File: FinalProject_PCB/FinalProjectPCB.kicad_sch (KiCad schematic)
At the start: 18 parts, among them J1 SerialJack, J2 Conn_01x09, SW1 SW_Push_Dual, SW2 SW_Push_Dual, SW3 SW_Push_Dual, SW4 SW_Push_Dual, SW5 SW_Push_Dual, SW6 SW_Push_Dual, SW7 SW_SPST, SW8 SW_Push_Dual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

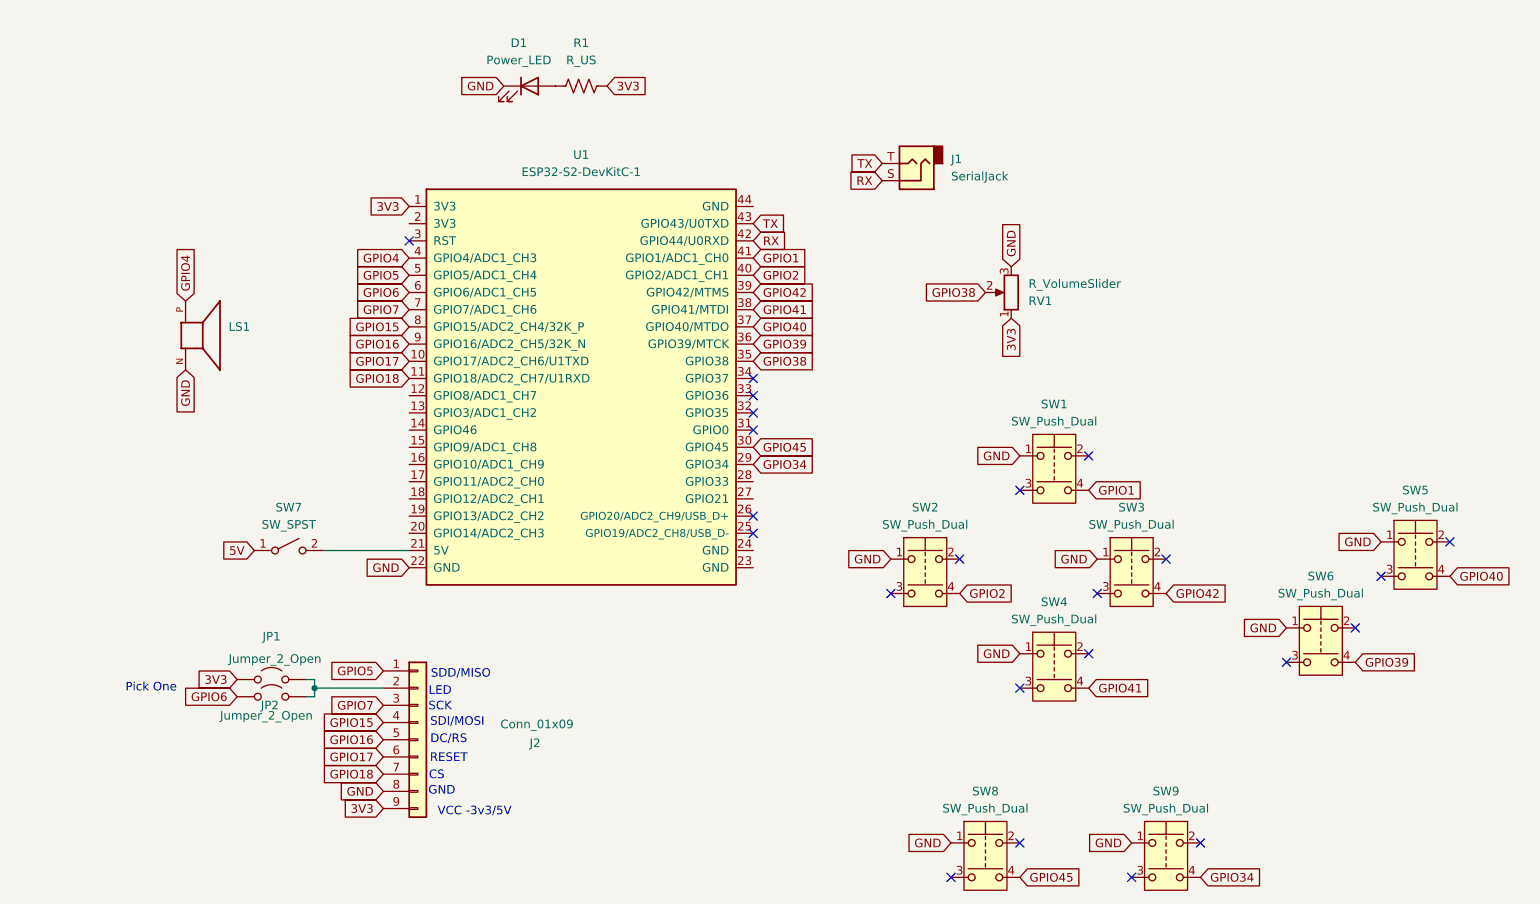
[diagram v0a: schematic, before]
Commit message: added GND pin to serial
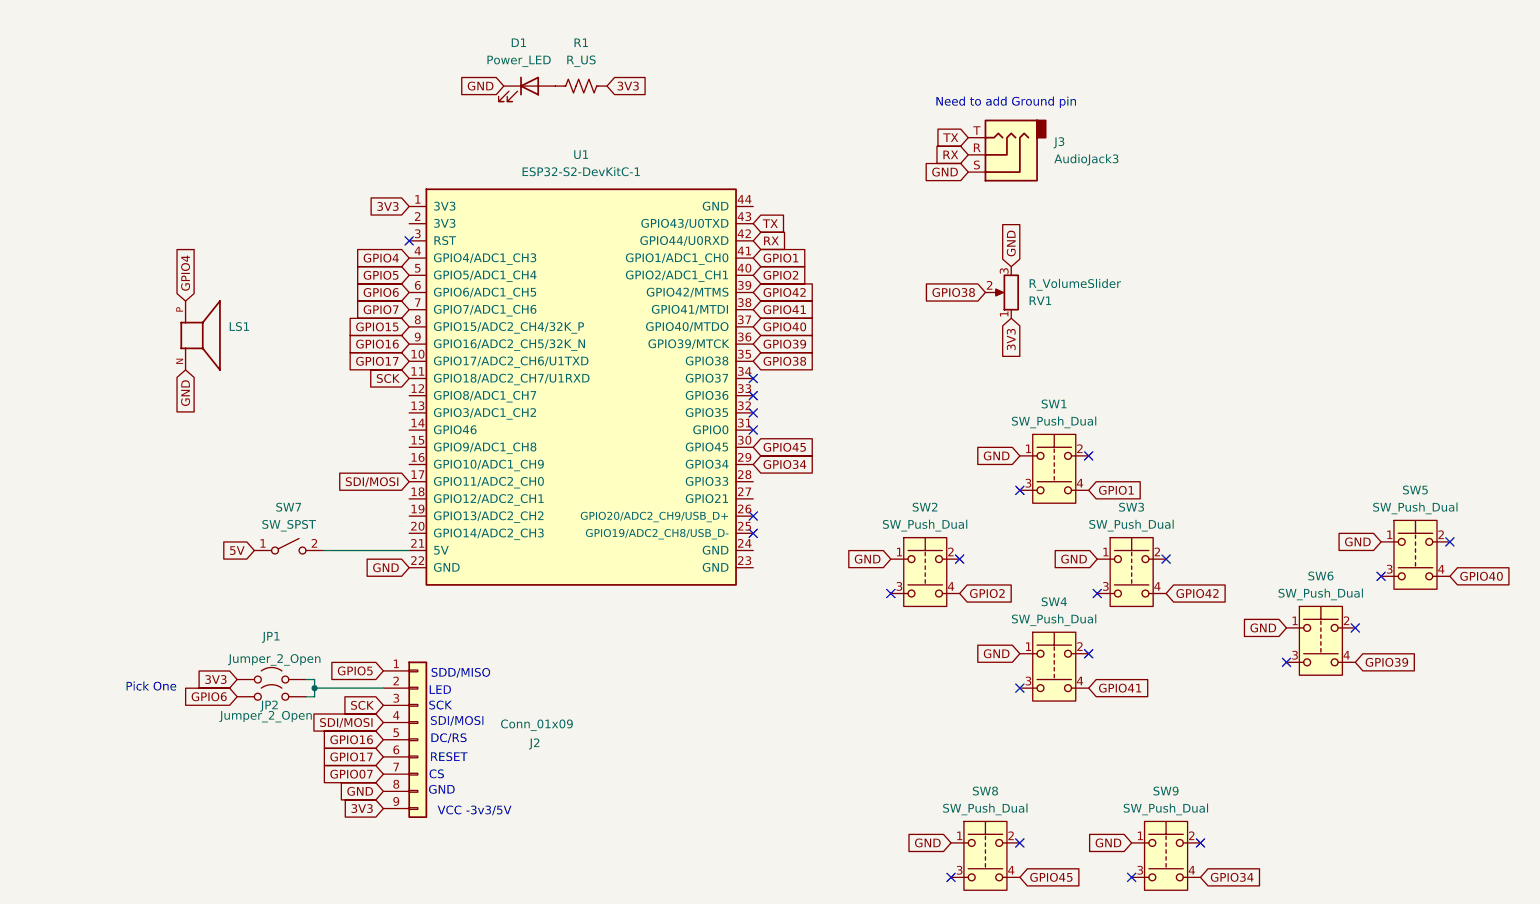
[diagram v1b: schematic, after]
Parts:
- removed J1: SerialJack, symbol Connector_Audio:AudioJack2
- added J3: AudioJack3, symbol Connector_Audio:AudioJack3
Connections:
- net GND: now also J3.S
- net GPIO15: no longer J2.4 (Pin_4)
- net GPIO7: no longer J2.3 (Pin_3)
- net RX: now also J3.R
- net TX: now also J3.T
- net SDI/MOSI: now reaches U1.17 (GPIO11/ADC2_CH0)
- net SDI/MOSI: now also J2.4 (Pin_4)
- net GPIO18 renamed GPIO07
- net GPIO07: no longer U1.11 (GPIO18/ADC2_CH7/U1RXD)
- new net SCK: J2.3 (Pin_3), U1.11 (GPIO18/ADC2_CH7/U1RXD)
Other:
- note added: "Need to add Ground pin"
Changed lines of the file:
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@@
+		)
+	)
+	(text "Need to add Ground pin"
+		(exclude_from_sim no)
+		(at 169.418 40.64 0)
+		(effects
+			(font
+				(size 1.27 1.27)
+			)
 		)
 	)
@@
 	(global_label "RX"
 		(shape input)
-		(at 151.13 52.07 180)
-		(fields_autoplaced yes)
-		(effects
-			(font
-				(size 1.27 1.27)
-			)
-			(justify right)
-		)
-		(property "Intersheetrefs" "${INTERSHEET_REFS}"
-			(at 145.6653 52.07 0)
+		(at 163.83 48.26 180)
+		(fields_autoplaced yes)
+		(effects
+			(font
+				(size 1.27 1.27)
+			)
+			(justify right)
+		)
+		(property "Intersheetrefs" "${INTERSHEET_REFS}"
+			(at 158.3653 48.26 0)
 			(effects
 				(font
@@
 		)
 	)
+	(global_label "SCK"
+		(shape input)
+		(at 81.28 81.28 180)
+		(fields_autoplaced yes)
+		(effects
+			(font
+				(size 1.27 1.27)
+			)
+			(justify right)
+		)
+		(property "Intersheetrefs" "${INTERSHEET_REFS}"
+			(at 74.5453 81.28 0)
+			(effects
+				(font
+					(size 1.27 1.27)
+				)
+				(justify right)
+				(hide yes)
+			)
+		)
+	)
 	(global_label "3V3"
 		(shape input)
@@
 		)
 	)
-	(global_label "GPIO18"
+	(global_label "GPIO07"
 		(shape input)
 		(at 77.47 139.7 180)
@@
 		)
 	)
-	(global_label "GPIO18"
-		(shape input)
-		(at 81.28 81.28 180)
-		(fields_autoplaced yes)
-		(effects
-			(font
-				(size 1.27 1.27)
-			)
-			(justify right)
-		)
-		(property "Intersheetrefs" "${INTERSHEET_REFS}"
-			(at 71.4005 81.28 0)
-			(effects
-				(font
-					(size 1.27 1.27)
-				)
-				(justify right)
-				(hide yes)
-			)
-		)
-	)
 	(global_label "TX"
 		(shape input)
-		(at 151.13 49.53 180)
-		(fields_autoplaced yes)
-		(effects
-			(font
-				(size 1.27 1.27)
-			)
-			(justify right)
-		)
-		(property "Intersheetrefs" "${INTERSHEET_REFS}"
-			(at 145.9677 49.53 0)
+		(at 163.83 45.72 180)
+		(fields_autoplaced yes)
+		(effects
+			(font
+				(size 1.27 1.27)
+			)
+			(justify right)
+		)
+		(property "Intersheetrefs" "${INTERSHEET_REFS}"
+			(at 158.6677 45.72 0)
 			(effects
 				(font
@@
 		)
 	)
+	(global_label "SDI{slash}MOSI"
+		(shape input)
+		(at 81.28 96.52 180)
+		(fields_autoplaced yes)
+		(effects
+			(font
+				(size 1.27 1.27)
+			)
+			(justify right)
+		)
+		(property "Intersheetrefs" "${INTERSHEET_REFS}"
+			(at 69.2838 96.52 0)
+			(effects
+				(font
+					(size 1.27 1.27)
+				)
+				(justify right)
+				(hide yes)
+			)
+		)
+	)
 	(global_label "GPIO4"
 		(shape input)
@@
 		)
 	)
+	(global_label "GND"
+		(shape input)
+		(at 163.83 50.8 180)
+		(fields_autoplaced yes)
+		(effects
+			(font
+				(size 1.27 1.27)
+			)
+			(justify right)
+		)
+		(property "Intersheetrefs" "${INTERSHEET_REFS}"
+			(at 156.9743 50.8 0)
+			(effects
+				(font
+					(size 1.27 1.27)
+				)
+				(justify right)
+				(hide yes)
+			)
+		)
+	)
 	(global_label "GPIO1"
 		(shape input)
@@
 		)
 	)
-	(global_label "GPIO7"
+	(global_label "SCK"
 		(shape input)
 		(at 77.47 129.54 180)
@@
 		)
 		(property "Intersheetrefs" "${INTERSHEET_REFS}"
-			(at 68.8 129.54 0)
-			(effects
-				(font
-					(size 1.27 1.27)
-				)
-				(justify right)
-				(hide yes)
-			)
-		)
-	)
-	(global_label "GPIO15"
+			(at 70.7353 129.54 0)
+			(effects
+				(font
+					(size 1.27 1.27)
+				)
+				(justify right)
+				(hide yes)
+			)
+		)
+	)
+	(global_label "SDI{slash}MOSI"
 		(shape input)
 		(at 77.47 132.08 180)
@@
 		)
 		(property "Intersheetrefs" "${INTERSHEET_REFS}"
-			(at 67.5905 132.08 0)
+			(at 65.4738 132.08 0)
 			(effects
 				(font
@@
 	)
 	(symbol
+		(lib_id "Connector_Audio:AudioJack3")
+		(at 168.91 48.26 180)
+		(unit 1)
+		(exclude_from_sim no)
+		(in_bom yes)
+		(on_board yes)
+		(dnp no)
+		(fields_autoplaced yes)
+		(property "Reference" "J3"
+			(at 176.53 46.3549 0)
+			(effects
+				(font
+					(size 1.27 1.27)
+				)
+				(justify right)
+			)
+		)
+		(property "Value" "AudioJack3"
+			(at 176.53 48.8949 0)
+			(effects
+				(font
+					(size 1.27 1.27)
+				)
+				(justify right)
+			)
+		)
+		(property "Footprint" ""
+			(at 168.91 48.26 0)
+			(effects
+				(font
+					(size 1.27 1.27)
+				)
+				(hide yes)
+			)
+		)
+		(property "Datasheet" "~"
+			(at 168.91 48.26 0)
+			(effects
+				(font
+					(size 1.27 1.27)
+				)
+				(hide yes)
+			)
+		)
+		(property "Description" "Audio Jack, 3 Poles (Stereo / TRS)"
+			(at 168.91 48.26 0)
+			(effects
+				(font
+					(size 1.27 1.27)
+				)
+				(hide yes)
+			)
+		)
+		(pin "R"
+		)
+		(pin "S"
+		)
+		(pin "T"
+		)
+		(instances
+			(project ""
+				(path "/779a3c99-a5a8-445d-8f38-e1d85c7e87cc"
+					(reference "J3")
+					(unit 1)
+				)
+			)
+		)
+	)
+	(symbol
 		(lib_id "Switch:SW_Push_Dual")
 		(at 229.87 107.95 0)
@@
 					(unit 1)
 				)
-			)
-		)
-	)
-	(symbol
-		(lib_id "Connector_Audio:AudioJack2")
-		(at 156.21 49.53 180)
-		(unit 1)
-		(exclude_from_sim no)
-		(in_bom yes)
-		(on_board yes)
-		(dnp no)
-		(fields_autoplaced yes)
-		(property "Reference" "J1"
-			(at 161.29 48.8949 0)
-			(effects
-				(font
-					(size 1.27 1.27)
-				)
-				(justify right)
-			)
-		)
-		(property "Value" "SerialJack"
-			(at 161.29 51.4349 0)
-			(effects
-				(font
-					(size 1.27 1.27)
-				)
-				(justify right)
-			)
-		)
-		(property "Footprint" ""
-			(at 156.21 49.53 0)
-			(effects
-				(font
-					(size 1.27 1.27)
-				)
-				(hide yes)
-			)
-		)
-		(property "Datasheet" "~"
-			(at 156.21 49.53 0)
-			(effects
-				(font
-					(size 1.27 1.27)
-				)
-				(hide yes)
-			)
-		)
-		(property "Description" "Audio Jack, 2 Poles (Mono / TS)"
-			(at 156.21 49.53 0)
-			(effects
-				(font
-					(size 1.27 1.27)
-				)
-				(hide yes)
-			)
-		)
-		(pin "T"
-		)
-		(pin "S"
-		)
-		(instances
-			(project ""
-				(path "/779a3c99-a5a8-445d-8f38-e1d85c7e87cc"
-					(reference "J1")
-					(unit 1)
-				)

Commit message: Updated Schematic to match working board
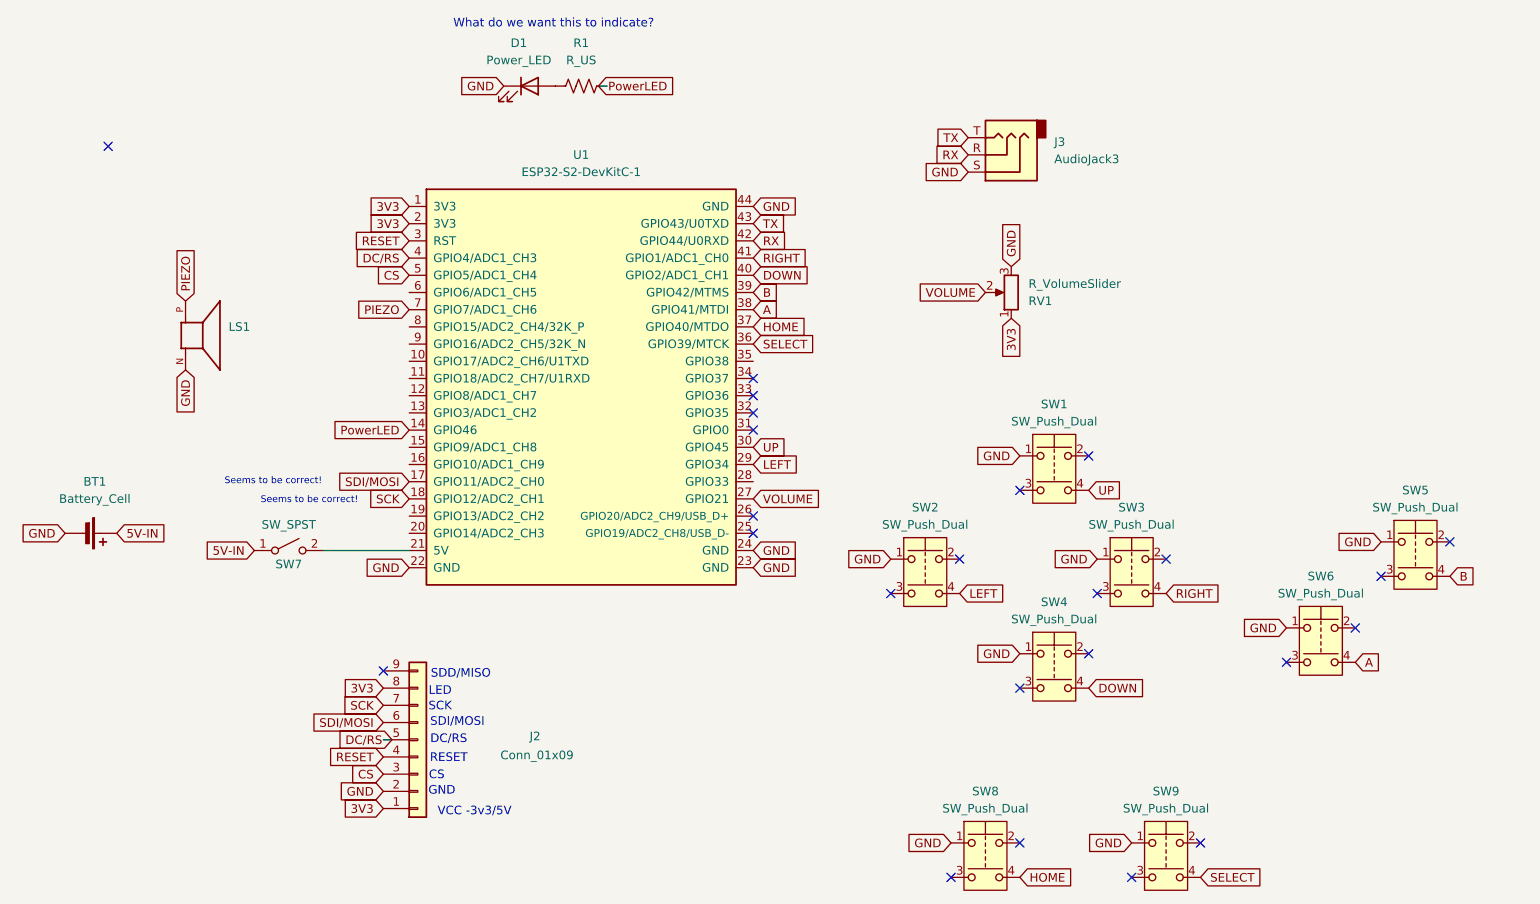
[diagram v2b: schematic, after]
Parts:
- removed JP1, JP2: Jumper_2_Open, symbol Jumper:Jumper_2_Open
- added BT1: Battery_Cell, symbol Device:Battery_Cell
- J2: footprint (none) -> TerminalBlock:TerminalBlock_Xinya_XY308-2.54-9P_1x09_P2.54mm_Horizontal
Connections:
- net GPIO07 is gone; now on net SCK: J2.7 (Pin_7)
- net 3V3: now also J2.1 (Pin_1), J2.8 (Pin_8), U1.2 (3V3); no longer J2.9 (Pin_9), R1.2
- net GND: now also J2.2 (Pin_2), U1.23 (GND), U1.24 (GND), U1.44 (GND), BT1.2 (-); no longer J2.8 (Pin_8)
- net SCK: now also U1.18 (GPIO12/ADC2_CH1); no longer J2.3 (Pin_3), U1.11 (GPIO18/ADC2_CH7/U1RXD)
- net SDI/MOSI: now also J2.6 (Pin_6); no longer J2.4 (Pin_4)
- net PowerLED: now reaches U1.14 (GPIO46)
- net PowerLED: now also R1.2
- net VOLUME: now reaches U1.27 (GPIO21)
- net VOLUME: now also RV1.2
- net RESET: now reaches U1.3 (RST)
- net RESET: now also J2.4 (Pin_4)
- net 5V renamed 5V-IN
- net 5V-IN: now also BT1.1 (+)
- net GPIO1 renamed RIGHT
- net RIGHT: now also SW3.4; no longer SW1.4
- net GPIO15: no longer names the net of U1.8 (GPIO15/ADC2_CH4/32K_P)
- net GPIO16: no longer names the net of U1.9 (GPIO16/ADC2_CH5/32K_N)
- net GPIO16: no longer J2.5 (Pin_5)
- net GPIO17: no longer names the net of U1.10 (GPIO17/ADC2_CH6/U1TXD)
- net GPIO17: no longer J2.6 (Pin_6)
- net GPIO2 renamed DOWN
- net DOWN: now also SW4.4; no longer SW2.4
- net GPIO34 renamed LEFT
- net LEFT: now also SW2.4; no longer SW9.4
- net GPIO38: no longer names the net of U1.35 (GPIO38)
- net GPIO38: no longer RV1.2
- net GPIO39 renamed A
- net A: now also U1.38 (GPIO41/MTDI); no longer U1.36 (GPIO39/MTCK)
- net GPIO4 renamed DC/RS
- net DC/RS: now also J2.5 (Pin_5); no longer LS1.P
- net GPIO40 renamed B
- net B: now also U1.39 (GPIO42/MTMS); no longer U1.37 (GPIO40/MTDO)
- removed net GPIO41: SW4.4, U1.38 (GPIO41/MTDI)
- removed net GPIO42: SW3.4, U1.39 (GPIO42/MTMS)
- net GPIO45 renamed HOME
- net HOME: now also U1.37 (GPIO40/MTDO); no longer U1.30 (GPIO45)
- net GPIO5 renamed CS
- net CS: now also J2.3 (Pin_3); no longer J2.1 (Pin_1)
- net GPIO6: no longer names the net of U1.6 (GPIO6/ADC1_CH5)
- net GPIO7 renamed PIEZO
- net PIEZO: now also LS1.P
- new net SELECT: SW9.4, U1.36 (GPIO39/MTCK)
- new net UP: SW1.4, U1.30 (GPIO45)
- no-connect marks 23 -> 24
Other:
- note added: "Seems to be correct!"
- note added: "What do we want this to indicate?"
- note removed: "Need to add Ground pin"
- note removed: "Pick One"

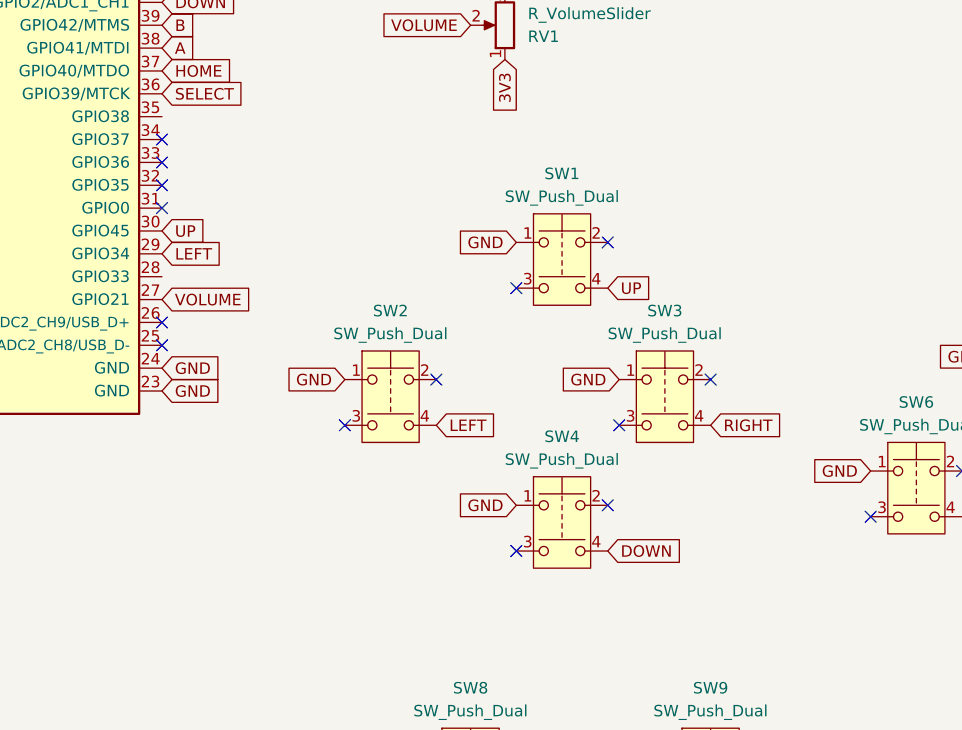
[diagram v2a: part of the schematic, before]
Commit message: added footprints
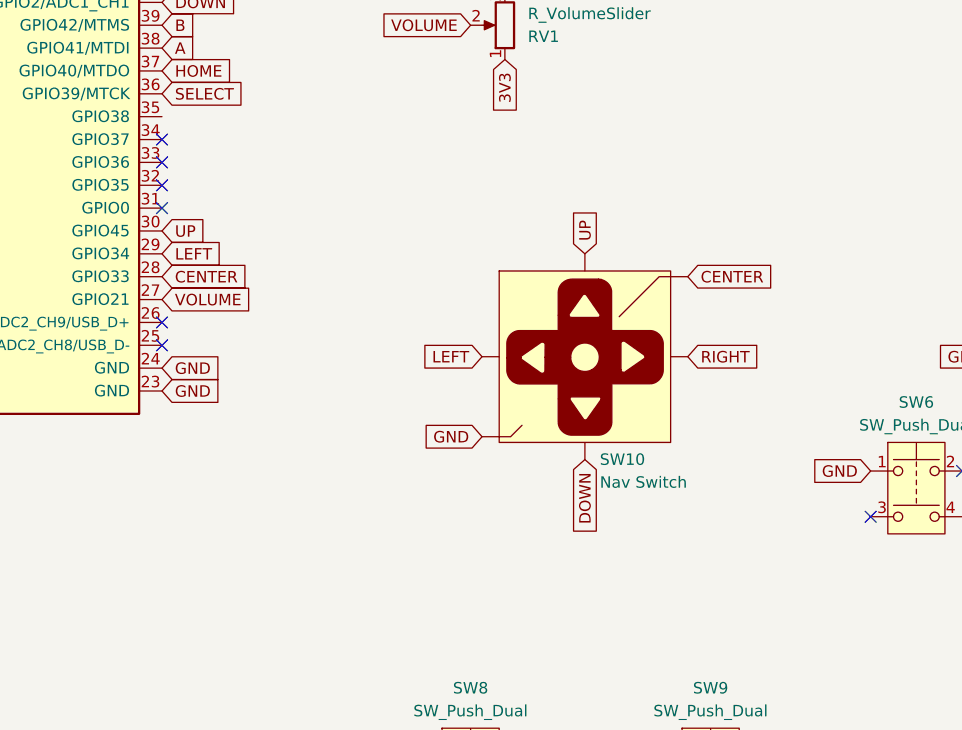
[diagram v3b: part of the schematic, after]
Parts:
- removed SW1, SW2, SW3, SW4: SW_Push_Dual, Button_Switch_THT:SW_PUSH-12mm, symbol Switch:SW_Push_Dual
- added SW10: Nav Switch, GooseCustom:Multi-Directional Switch 5 Position, symbol SparkFun-Switch:Navigation_5Way_SMD_9.9x9.9mm
- BT1, J3: footprint (none) -> Connector_PinHeader_1.00mm:PinHeader_1x03_P1.00mm_Vertical
- R1: footprint (none) -> Resistor_THT:R_Axial_DIN0204_L3.6mm_D1.6mm_P5.08mm_Horizontal
- RV1: footprint (none) -> GooseCustom:Thumb_TRIM_3352T-1-104LF
- SW5, SW6, SW8, SW9: footprint Button_Switch_THT:SW_PUSH-12mm -> GooseCustom:D6R90_CNK Button
- SW7: footprint (none) -> TestPoint:TestPoint_Bridge_Pitch2.54mm_Drill1.0mm
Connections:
- net DOWN: now also SW10.5 (Down)
- net GND: now also SW10.10 (GND), SW10.3 (GND), SW10.6 (GND), SW10.8 (GND), SW10.9 (GND)
- net LEFT: now also SW10.7 (Left)
- net RIGHT: now also SW10.2 (Right)
- net UP: now also SW10.1 (Up)
- net CENTER: now reaches U1.28 (GPIO33)
- net CENTER: now also SW10.4 (Center)
- no-connect marks 24 -> 16

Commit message: Started PCB
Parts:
- removed J3: AudioJack3, Connector_PinHeader_1.00mm:PinHeader_1x03_P1.00mm_Vertical, symbol Connector_Audio:AudioJack3
- added J1: Serial Jack, TerminalBlock:TerminalBlock_Xinya_XY308-2.54-3P_1x03_P2.54mm_Horizontal, symbol Connector_Generic:Conn_01x03
- BT1: footprint Connector_PinHeader_1.00mm:PinHeader_1x03_P1.00mm_Vertical -> TerminalBlock:TerminalBlock_Xinya_XY308-2.54-2P_1x02_P2.54mm_Horizontal
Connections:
- net GND: now also J1.1 (Pin_1)
- net RX: now also J1.3 (Pin_3)
- net TX: now also J1.2 (Pin_2)
- no-connect marks 16 -> 15

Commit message: Finished PCB
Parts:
- SW7: footprint TestPoint:TestPoint_Bridge_Pitch2.54mm_Drill1.0mm -> TerminalBlock:TerminalBlock_Xinya_XY308-2.54-2P_1x02_P2.54mm_Horizontal
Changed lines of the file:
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@@
 			)
 		)
-		(property "Footprint" "TestPoint:TestPoint_Bridge_Pitch2.54mm_Drill1.0mm"
+		(property "Footprint" "TerminalBlock:TerminalBlock_Xinya_XY308-2.54-2P_1x02_P2.54mm_Horizontal"
 			(at 63.5 106.68 0)
 			(effects
